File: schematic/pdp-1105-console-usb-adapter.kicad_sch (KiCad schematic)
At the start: 10 parts, among them J1 Console Connector, J2 TTY RS-232 Connector, U1 Teensy 3.1/3.2, U2 MAX202

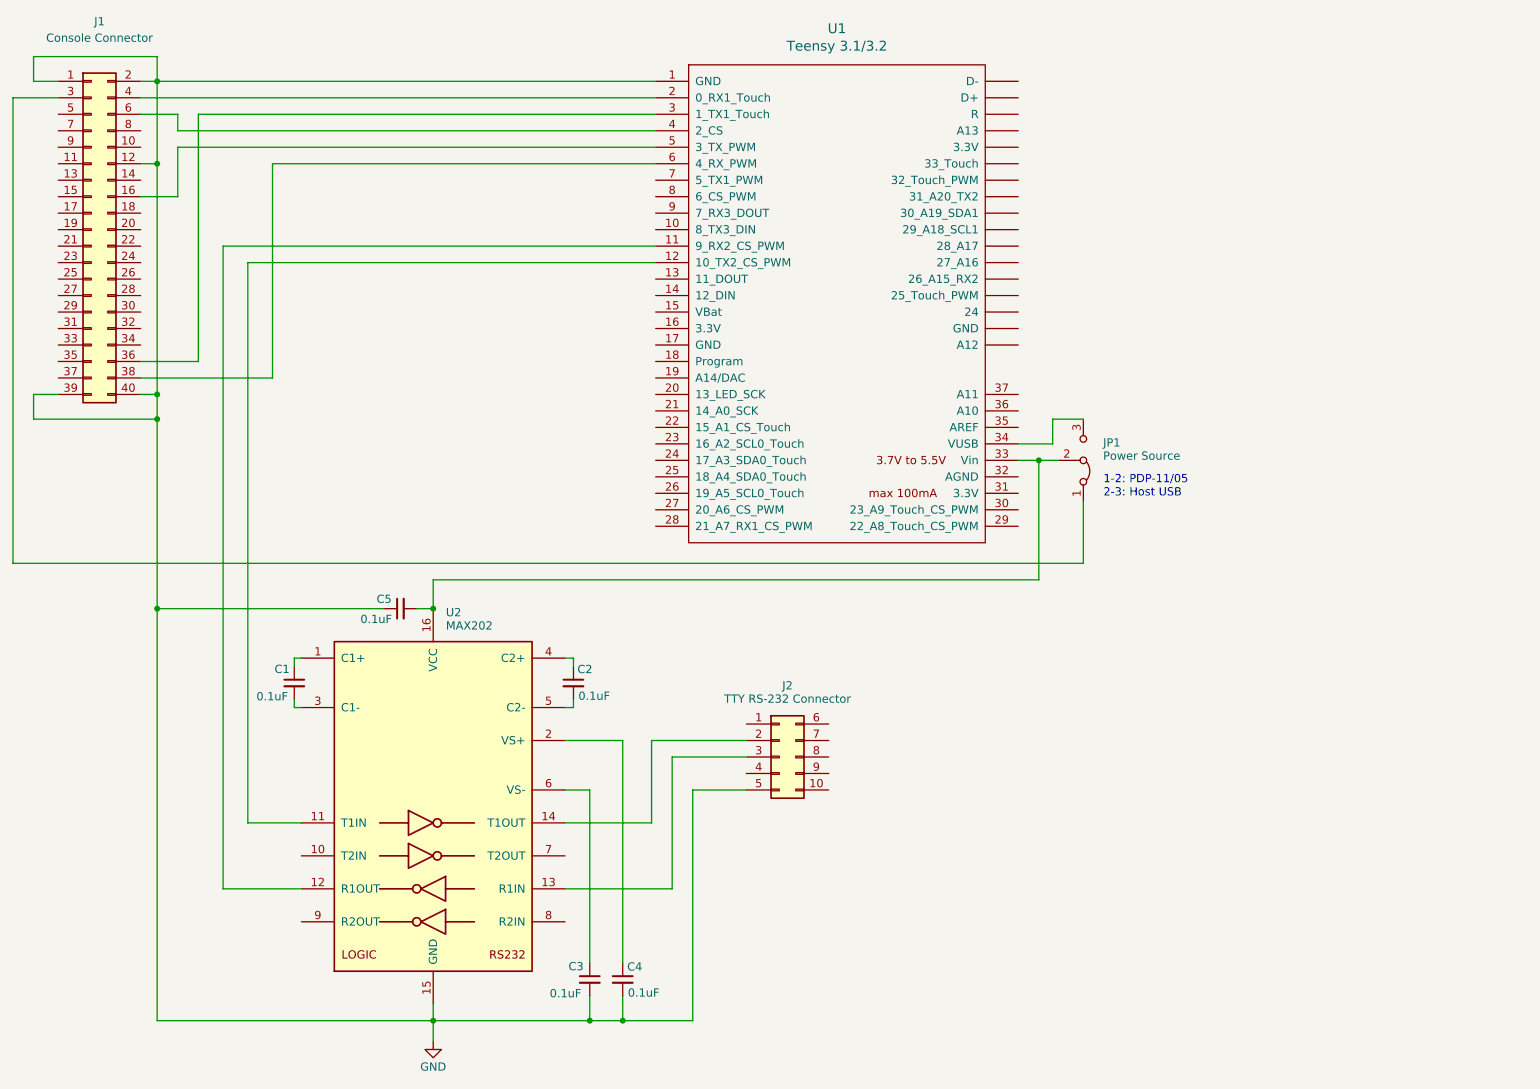
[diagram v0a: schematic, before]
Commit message: Simplified power circuit and updated documentation
-- Eliminated the jumper used to select between USB and PDP-11 power in favor
of always sourcing power from the PDP.  With this change, one must now use a
wire jumper between VUSB and pin 3 on the console connector to power the
adapter from the USB host.  This simplifies construction and has the added
benefit of making it essentially impossible to mistakenly connect USB +5V to
the PDP-11’s +5V line.

-- Updated the README to reflect the new power circuit design. Added new
sections describing how to modify the Teensy for use with external power and
how to power the adapter from USB.

-- Revised all the README images to show the latest example design.

-- Added README section on building the aux terminal cable.

-- Rearranged the order of sections for clarity and made various other
editorial changes.
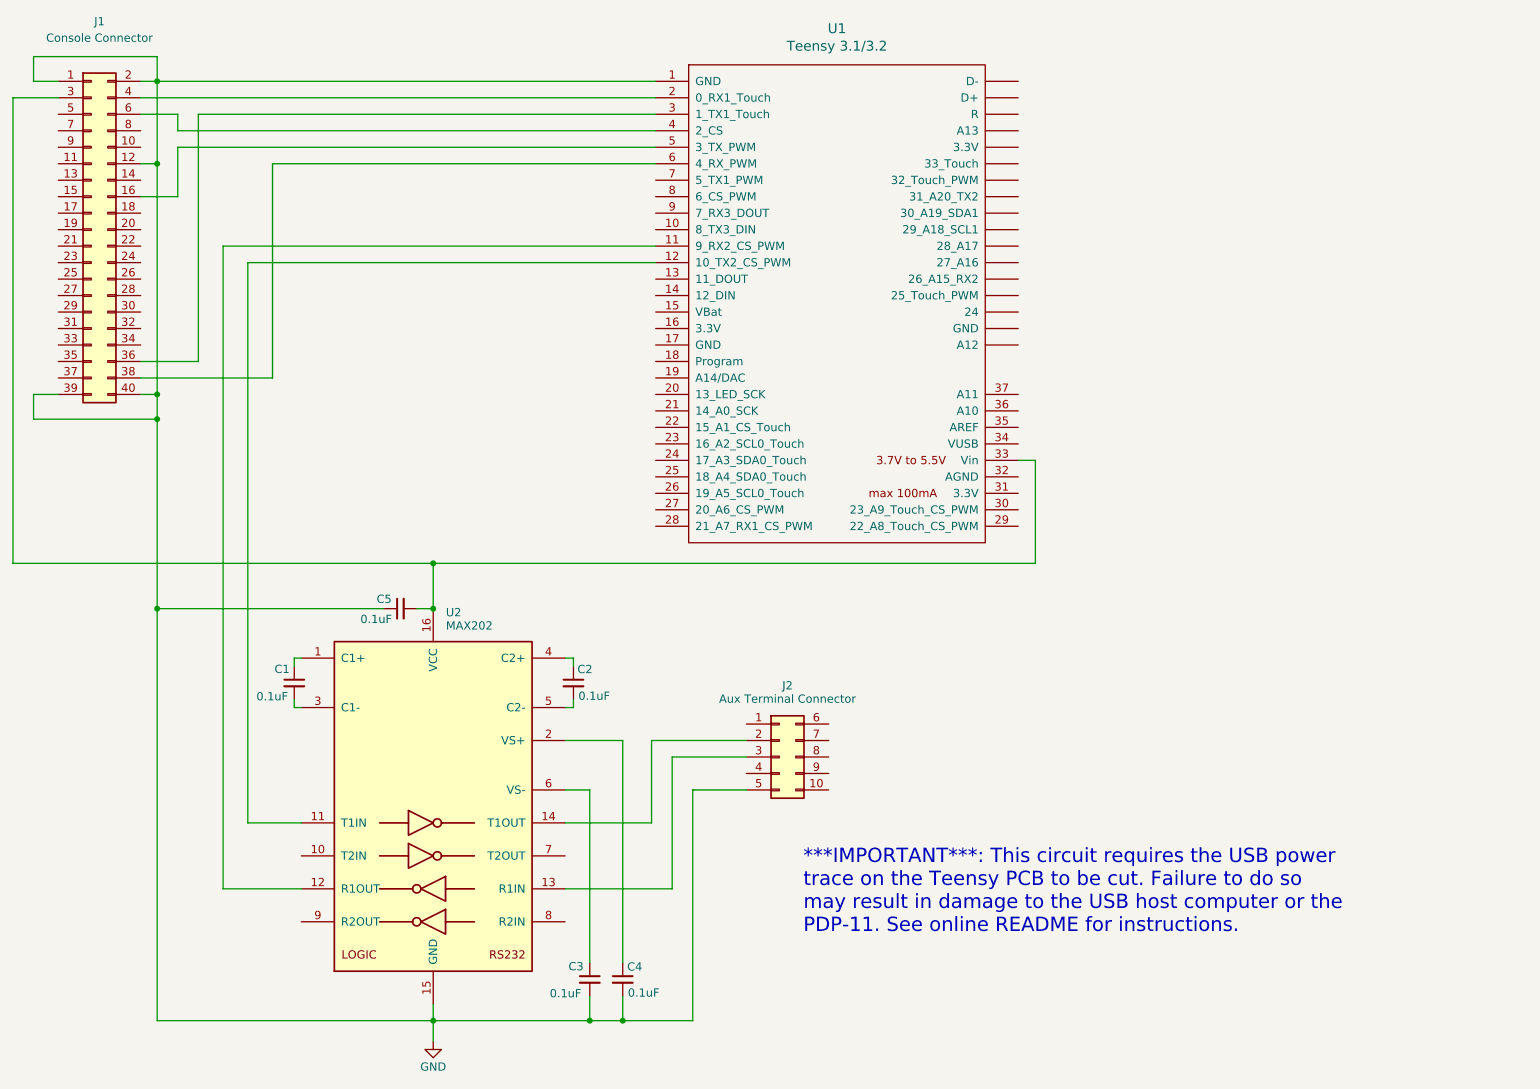
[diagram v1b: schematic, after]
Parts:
- removed JP1: Power Source, symbol Jumper:Jumper_3_Bridged12
- J2: value TTY RS-232 Connector -> Aux Terminal Connector
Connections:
- net at C5.2, U1.33 (Vin), U2.16 (VCC): now also J1.3 (Pin_3)
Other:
- note added: "***IMPORTANT***: This circuit requires the USB power trace on the Teensy PCB to be cut. Failure to do so may result in damage to the USB host computer or the PDP-11. See online README for instructions."
- note removed: "1-2: PDP-11/05 2-3: Host USB"
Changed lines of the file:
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@@
   (title_block
     (title "PDP-11/05 Console USB Adapter")
-    (date "2023-06-26")
-    (rev "2.0")
+    (date "2023-11-19")
+    (rev "3.0")
     (comment 1 "Licensed under a Creative Commons Attribution 4.0 International License")
     (comment 2 "Copyright © 2023 Jay Logue")
+    (comment 4 "https://github.com/jaylogue/pdp-1105-console-usb-adapter")
   )
   (junction (at 112.395 118.745) (diameter 0) (color 0 0 0 0)
   )
-  (junction (at 205.74 95.885) (diameter 0) (color 0 0 0 0)
-  )
   (junction (at 69.85 89.535) (diameter 0) (color 0 0 0 0)
   )
   (junction (at 112.395 182.245) (diameter 0) (color 0 0 0 0)
   )
+  (junction (at 112.395 111.76) (diameter 0) (color 0 0 0 0)
+  )
   (junction (at 69.85 118.745) (diameter 0) (color 0 0 0 0)
   )
@@
     (stroke (width 0) (type default))
   )
+  (wire (pts (xy 112.395 111.76) (xy 112.395 118.745))
+    (stroke (width 0) (type default))
+  )
   (wire (pts (xy 134.0104 126.365) (xy 134.0104 127.6604))
     (stroke (width 0) (type default))
@@
     (stroke (width 0) (type default))
   )
+  (wire (pts (xy 205.2066 95.885) (xy 205.2066 111.76))
+    (stroke (width 0) (type default))
+  )
   (wire (pts (xy 50.8 85.725) (xy 50.8 89.535))
     (stroke (width 0) (type default))
@@
     (stroke (width 0) (type default))
   )
-  (wire (pts (xy 207.8736 89.535) (xy 212.598 89.535))
+  (wire (pts (xy 202.565 95.885) (xy 205.2066 95.885))
     (stroke (width 0) (type default))
   )
@@
     (stroke (width 0) (type default))
   )
-  (wire (pts (xy 212.598 102.235) (xy 212.598 111.76))
-    (stroke (width 0) (type default))
-  )
   (wire (pts (xy 73.025 55.245) (xy 67.31 55.245))
     (stroke (width 0) (type default))
@@
     (stroke (width 0) (type default))
   )
-  (wire (pts (xy 112.395 118.745) (xy 112.395 114.3))
-    (stroke (width 0) (type default))
-  )
-  (wire (pts (xy 205.74 95.885) (xy 208.788 95.885))
+  (wire (pts (xy 112.395 111.76) (xy 47.625 111.76))
     (stroke (width 0) (type default))
   )
@@
     (stroke (width 0) (type default))
   )
-  (wire (pts (xy 202.565 95.885) (xy 205.74 95.885))
-    (stroke (width 0) (type default))
-  )
   (wire (pts (xy 73.025 42.545) (xy 73.025 45.085))
     (stroke (width 0) (type default))
@@
     (stroke (width 0) (type default))
   )
-  (wire (pts (xy 112.395 114.3) (xy 205.74 114.3))
-    (stroke (width 0) (type default))
-  )
   (wire (pts (xy 136.525 182.245) (xy 112.395 182.245))
     (stroke (width 0) (type default))
@@
     (stroke (width 0) (type default))
   )
-  (wire (pts (xy 207.8736 93.345) (xy 207.8736 89.535))
-    (stroke (width 0) (type default))
-  )
   (wire (pts (xy 80.01 161.925) (xy 80.01 62.865))
     (stroke (width 0) (type default))
@@
     (stroke (width 0) (type default))
   )
+  (wire (pts (xy 205.2066 111.76) (xy 112.395 111.76))
+    (stroke (width 0) (type default))
+  )
   (wire (pts (xy 146.05 139.065) (xy 160.655 139.065))
     (stroke (width 0) (type default))
@@
     (stroke (width 0) (type default))
   )
-  (wire (pts (xy 202.565 93.345) (xy 207.8736 93.345))
-    (stroke (width 0) (type default))
-  )
   (wire (pts (xy 132.715 126.365) (xy 134.0104 126.365))
     (stroke (width 0) (type default))
@@
     (stroke (width 0) (type default))
   )
-  (wire (pts (xy 205.74 114.3) (xy 205.74 95.885))
-    (stroke (width 0) (type default))
-  )
   (wire (pts (xy 80.01 62.865) (xy 146.685 62.865))
     (stroke (width 0) (type default))
@@
     (stroke (width 0) (type default))
   )
-  (wire (pts (xy 212.598 111.76) (xy 47.625 111.76))
-    (stroke (width 0) (type default))
-  )
   (wire (pts (xy 92.075 133.985) (xy 90.9828 133.985))
     (stroke (width 0) (type default))
@@
     (stroke (width 0) (type default))
   )
-  (text "1-2: PDP-11/05\n2-3: Host USB" (at 215.6968 101.7016 0)
-    (effects (font (size 1.27 1.27) (color 0 132 132 1)) (justify left bottom))
+  (text "***IMPORTANT***: This circuit requires the USB power\ntrace on the Teensy PCB to be cut. Failure to do so\nmay result in damage to the USB host computer or the\nPDP-11. See online README for instructions."
+    (at 169.4434 168.9354 0)
+    (effects (font (face "Arial") (size 2.2 2.2) (color 0 0 0 1)) (justify left bottom))
   )
   (symbol (lib_id "pdp-1105-console-usb-adapter-rescue:Teensy3.1-teensy") (at 174.625 71.755 0) (unit 1)
@@
       (effects (font (size 1.27 1.27)))
     )
-    (property "Value" "TTY RS-232 Connector" (at 167.005 132.6548 0)
+    (property "Value" "Aux Terminal Connector" (at 167.005 132.6548 0)
       (effects (font (size 1.27 1.27)))
     )
@@
         )
       )
-    )
-  )
-  (symbol (lib_id "Jumper:Jumper_3_Bridged12") (at 212.598 95.885 270) (mirror x) (unit 1)
-    (in_bom yes) (on_board yes) (dnp no)
-    (property "Reference" "JP1" (at 215.646 93.1672 90)
-      (effects (font (size 1.27 1.27)) (justify left))
-    )
-    (property "Value" "Power Source" (at 215.646 95.1992 90)
-      (effects (font (size 1.27 1.27)) (justify left))
-    )
-    (property "Footprint" "" (at 212.598 95.885 0)
-      (effects (font (size 1.27 1.27)) hide)
-    )
-    (property "Datasheet" "~" (at 212.598 95.885 0)
-      (effects (font (size 1.27 1.27)) hide)
-    )
-    (pin "1")
-    (pin "2")
-    (pin "3")
-    (instances
-      (project "pdp-1105-console-usb-adapter"
-        (path "/d2a3b5f2-ee0f-40f3-9959-bd44e9d6ebec"
-          (reference "JP1") (unit 1)
-        )
-      )
